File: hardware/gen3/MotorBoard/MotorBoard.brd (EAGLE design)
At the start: 140 x 107 mm, 193 parts, among them U2 ATMEGA165PV-8AU

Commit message: fixed ERCs on all boards
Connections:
- new net N$45: R2.2, SPI_HEADER.1
- net 5V: now also U$5.5, U$6.5, U$7.5, U$8.5; no longer U$5.2, U$6.2, U$7.2, U$8.2
- net GND: now also U$5.2, U$6.2, U$7.2, U$8.2; no longer U$5.5, U$6.5, U$7.5, U$8.5
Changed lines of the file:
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@@
 <contactref element="C15" pad="1"/>
 <contactref element="C24" pad="1"/>
-<contactref element="U$5" pad="5"/>
 <contactref element="R90" pad="1"/>
 <contactref element="C33" pad="1"/>
@@
 <contactref element="LED13" pad="C"/>
 <contactref element="LED15" pad="C"/>
-<contactref element="U$6" pad="5"/>
-<contactref element="U$7" pad="5"/>
 <contactref element="R60" pad="1"/>
-<contactref element="U$8" pad="5"/>
 <contactref element="R62" pad="1"/>
 <contactref element="R58" pad="1"/>
+<contactref element="U$5" pad="2"/>
+<contactref element="U$6" pad="2"/>
+<contactref element="U$7" pad="2"/>
+<contactref element="U$8" pad="2"/>
 <wire x1="137" y1="25.86" x2="137" y2="79.86" width="0" layer="19" extent="1-1"/>
 <wire x1="100.0766" y1="38.191" x2="137" y2="25.86" width="0" layer="19" extent="1-1"/>
@@
 <wire x1="24" y1="57" x2="52.77" y2="54.98" width="0" layer="19" extent="1-1"/>
 <wire x1="24" y1="59.54" x2="24" y2="57" width="0" layer="19" extent="1-1"/>
-<wire x1="14.43" y1="62.8801" x2="24" y2="59.54" width="0" layer="19" extent="16-16"/>
-<wire x1="14.17" y1="63.58" x2="14.43" y2="62.8801" width="0" layer="19" extent="16-16"/>
+<wire x1="13.48" y1="60.2799" x2="24" y2="59.54" width="0" layer="19" extent="16-16"/>
+<wire x1="14.17" y1="63.58" x2="13.48" y2="60.2799" width="0" layer="19" extent="16-16"/>
 <wire x1="13.73" y1="64.58" x2="14.17" y2="63.58" width="0" layer="19" extent="16-16"/>
 <wire x1="14.25" y1="65.58" x2="13.73" y2="64.58" width="0" layer="19" extent="16-16"/>
@@
 <wire x1="8.14" y1="75.52" x2="6.98" y2="74.52" width="0" layer="19" extent="16-16"/>
 <wire x1="6.82" y1="77.52" x2="8.14" y2="75.52" width="0" layer="19" extent="16-16"/>
-<wire x1="11.97" y1="52.71" x2="14.43" y2="62.8801" width="0" layer="19" extent="16-16"/>
+<wire x1="11.97" y1="52.71" x2="13.48" y2="60.2799" width="0" layer="19" extent="16-16"/>
 <wire x1="14.42" y1="49.9" x2="11.97" y2="52.71" width="0" layer="19" extent="16-16"/>
 <wire x1="8.16" y1="52.71" x2="11.97" y2="52.71" width="0" layer="19" extent="16-16"/>
@@
 <wire x1="16.35" y1="5.895" x2="13.429" y2="2.9234" width="0" layer="19" extent="16-16"/>
 <wire x1="63.34" y1="4.99" x2="97.105" y2="35.27" width="0" layer="19" extent="1-1"/>
-<wire x1="-96.95" y1="-1.6999" x2="1.569" y2="2.9234" width="0" layer="19" extent="1-16"/>
-<wire x1="-96.4" y1="-11" x2="-96.95" y2="-1.6999" width="0" layer="19" extent="1-1"/>
-<wire x1="-96.95" y1="-18.6999" x2="-96.4" y2="-11" width="0" layer="19" extent="1-1"/>
-<wire x1="-96.4" y1="-28" x2="-96.95" y2="-18.6999" width="0" layer="19" extent="1-1"/>
-<wire x1="-96.95" y1="-35.6999" x2="-96.4" y2="-28" width="0" layer="19" extent="1-1"/>
-<wire x1="-96.4" y1="-45" x2="-96.95" y2="-35.6999" width="0" layer="19" extent="1-1"/>
+<wire x1="-96" y1="-4.3001" x2="1.569" y2="2.9234" width="0" layer="19" extent="1-16"/>
+<wire x1="-96.4" y1="-11" x2="-96" y2="-4.3001" width="0" layer="19" extent="1-1"/>
+<wire x1="-96" y1="-21.3001" x2="-96.4" y2="-11" width="0" layer="19" extent="1-1"/>
+<wire x1="-96.4" y1="-28" x2="-96" y2="-21.3001" width="0" layer="19" extent="1-1"/>
+<wire x1="-96" y1="-38.3001" x2="-96.4" y2="-28" width="0" layer="19" extent="1-1"/>
+<wire x1="-96.4" y1="-45" x2="-96" y2="-38.3001" width="0" layer="19" extent="1-1"/>
 </signal>
 <signal name="3.3V">
@@
 <contactref element="R75" pad="2"/>
 <contactref element="R74" pad="2"/>
-<contactref element="U$5" pad="2"/>
-<contactref element="U$6" pad="2"/>
-<contactref element="U$7" pad="2"/>
-<contactref element="U$8" pad="2"/>
+<contactref element="U$5" pad="5"/>
+<contactref element="U$6" pad="5"/>
+<contactref element="U$7" pad="5"/>
+<contactref element="U$8" pad="5"/>
 <wire x1="137" y1="23.32" x2="137" y2="77.32" width="0" layer="19" extent="1-1"/>
 <wire x1="64.1" y1="60.61" x2="137" y2="77.32" width="0" layer="19" extent="1-1"/>
@@
 <wire x1="24" y1="67.16" x2="52.77" y2="52.44" width="0" layer="19" extent="1-1"/>
 <wire x1="24" y1="69.7" x2="24" y2="67.16" width="0" layer="19" extent="1-1"/>
-<wire x1="13.48" y1="60.2799" x2="24" y2="67.16" width="0" layer="19" extent="16-16"/>
-<wire x1="11.62" y1="46.09" x2="13.48" y2="60.2799" width="0" layer="19" extent="16-16"/>
+<wire x1="14.43" y1="62.8801" x2="24" y2="67.16" width="0" layer="19" extent="16-16"/>
+<wire x1="16.7" y1="46.09" x2="14.43" y2="62.8801" width="0" layer="19" extent="16-16"/>
+<wire x1="16.38" y1="45.09" x2="16.7" y2="46.09" width="0" layer="19" extent="16-16"/>
+<wire x1="16.02" y1="45.09" x2="16.38" y2="45.09" width="0" layer="19" extent="16-16"/>
+<wire x1="11.62" y1="46.09" x2="16.02" y2="45.09" width="0" layer="19" extent="16-16"/>
 <wire x1="11.26" y1="45.09" x2="11.62" y2="46.09" width="0" layer="19" extent="16-16"/>
 <wire x1="10.94" y1="45.09" x2="11.26" y2="45.09" width="0" layer="19" extent="16-16"/>
-<wire x1="16.02" y1="45.09" x2="11.62" y2="46.09" width="0" layer="19" extent="16-16"/>
-<wire x1="16.38" y1="45.09" x2="16.02" y2="45.09" width="0" layer="19" extent="16-16"/>
-<wire x1="16.7" y1="46.09" x2="16.38" y2="45.09" width="0" layer="19" extent="16-16"/>
 <wire x1="6.54" y1="46.09" x2="10.94" y2="45.09" width="0" layer="19" extent="16-16"/>
 <wire x1="6.18" y1="45.09" x2="6.54" y2="46.09" width="0" layer="19" extent="16-16"/>
@@
 <wire x1="1.1" y1="45.09" x2="1.46" y2="46.09" width="0" layer="19" extent="16-16"/>
 <wire x1="0.78" y1="45.09" x2="1.1" y2="45.09" width="0" layer="19" extent="16-16"/>
-<wire x1="-96" y1="-4.3001" x2="0.78" y2="45.09" width="0" layer="19" extent="1-16"/>
-<wire x1="-96" y1="-21.3001" x2="-96" y2="-4.3001" width="0" layer="19" extent="1-1"/>
-<wire x1="-96" y1="-38.3001" x2="-96" y2="-21.3001" width="0" layer="19" extent="1-1"/>
+<wire x1="-96.95" y1="-1.6999" x2="0.78" y2="45.09" width="0" layer="19" extent="1-16"/>
+<wire x1="-96.95" y1="-18.6999" x2="-96.95" y2="-1.6999" width="0" layer="19" extent="1-1"/>
+<wire x1="-96.95" y1="-35.6999" x2="-96.95" y2="-18.6999" width="0" layer="19" extent="1-1"/>
 </signal>
 <signal name="M1QB">
@@
 <wire x1="62.38" y1="90.9934" x2="116" y2="72.38" width="0" layer="19" extent="1-1"/>
 </signal>
+<signal name="N$45">
+<contactref element="SPI_HEADER" pad="1"/>
+<contactref element="R2" pad="2"/>
+<wire x1="13.98" y1="52.71" x2="116" y2="80" width="0" layer="19" extent="16-16"/>
+</signal>
 </signals>

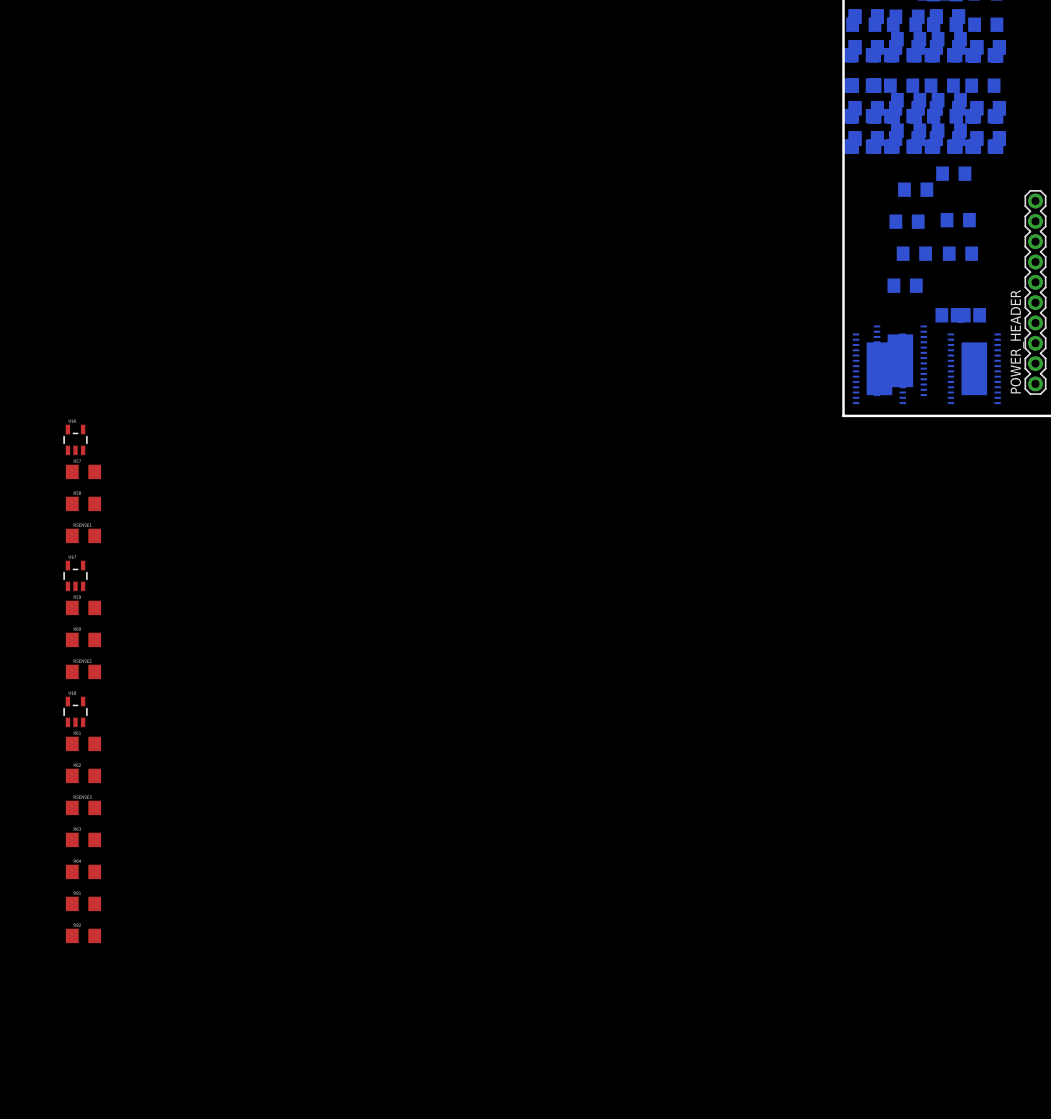
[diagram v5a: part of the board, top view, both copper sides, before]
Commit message: new overcurrent protection of pwm
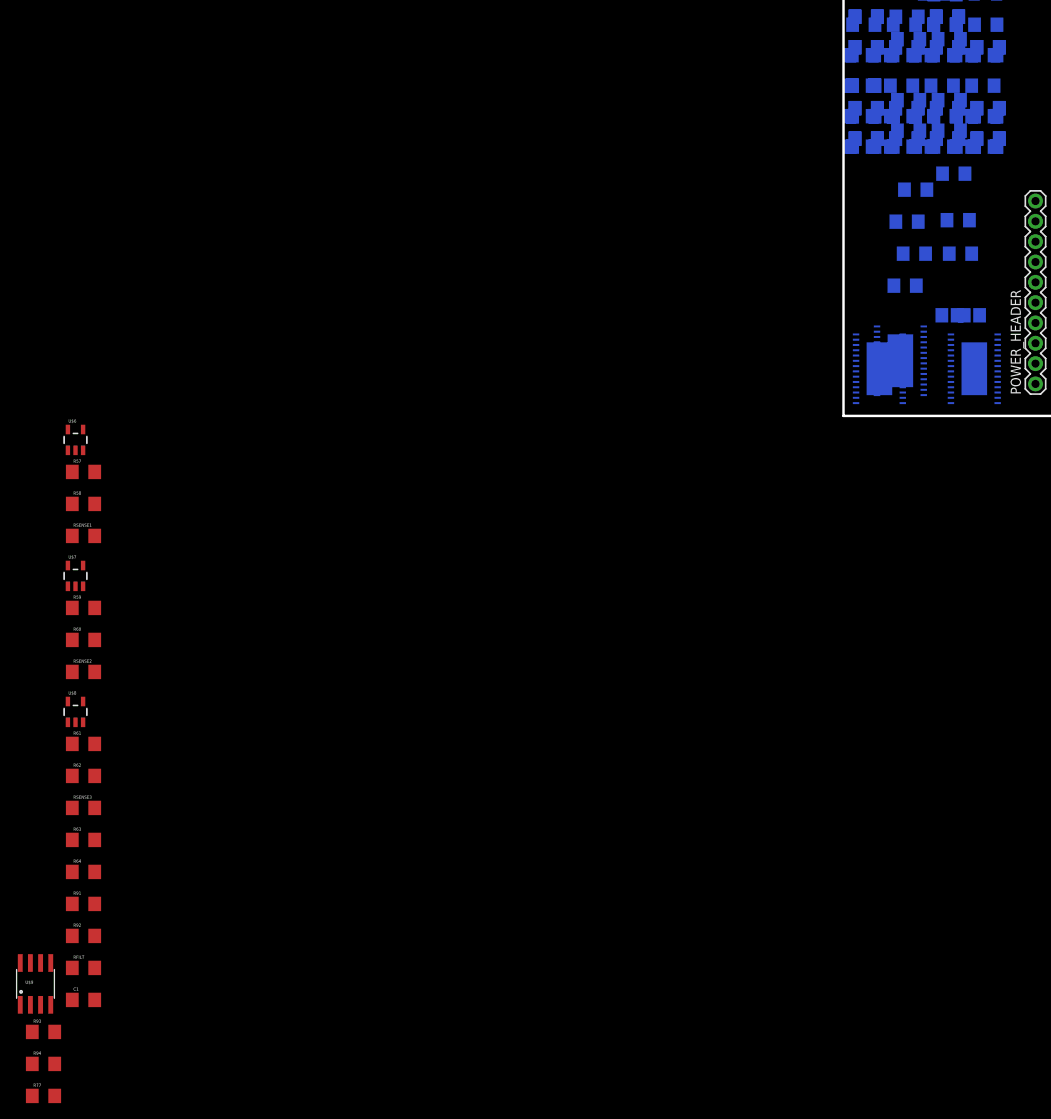
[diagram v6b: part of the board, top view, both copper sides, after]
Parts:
- added C1: .1uF, SparkFun-Passives:1206
- added R93: 64k, SparkFun-Resistors:1206
- added R94: 36k, SparkFun-Resistors:1206
- added RFILT: 15k, SparkFun-Resistors:1206
- added U$9: LM393, SparkFun-AnalogIC:SO08
- R77: value 1k -> 3k
- moved R77 175.5 mm to (-100.0, -85.0), flipped to the top
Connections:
- removed net N$97: R77.1, U$4.ENABLE
- new net LIM1: R77.2, U$4.ENABLE, U$9.1
- new net N$46: C1.1, RFILT.2, U$5.3
- new net N$66: R93.1, R94.2, U$9.2
- net 5V: now also R93.2, U$9.8
- net GND: now also C1.2, R94.1, U$9.4
- net O1: now also RFILT.1; no longer U$5.3
- net PWM1: now also R77.1; no longer R77.2
- net SENSE1: now also U$9.3
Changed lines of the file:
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@@
 <element name="R75" library="SparkFun-Resistors" package="1206" value="10k" x="7.58" y="45.09" rot="MR0"/>
 <element name="R76" library="SparkFun-Resistors" package="1206" value="10k" x="12.66" y="45.09" rot="MR0"/>
-<element name="R77" library="SparkFun-Resistors" package="1206" value="1k" x="17.74" y="45.09" rot="MR0"/>
 <element name="R78" library="SparkFun-Resistors" package="1206" value="1k" x="2.82" y="46.09" rot="MR0"/>
 <element name="R79" library="SparkFun-Resistors" package="1206" value="1k" x="7.9" y="46.09" rot="MR0"/>
@@
 <element name="R91" library="SparkFun-Resistors" package="1206" value="1k" x="-95" y="-61"/>
 <element name="R92" library="SparkFun-Resistors" package="1206" value="1k" x="-95" y="-65"/>
+<element name="RFILT" library="SparkFun-Resistors" package="1206" value="15k" x="-95" y="-69"/>
+<element name="C1" library="SparkFun-Passives" package="1206" value=".1uF" x="-95" y="-73"/>
+<element name="U$9" library="SparkFun-AnalogIC" package="SO08" value="LM393" x="-101" y="-71"/>
+<element name="R93" library="SparkFun-Resistors" package="1206" value="64k" x="-100" y="-77"/>
+<element name="R94" library="SparkFun-Resistors" package="1206" value="36k" x="-100" y="-81"/>
+<element name="R77" library="SparkFun-Resistors" package="1206" value="3k" x="-100" y="-85"/>
 </elements>
 <signals>
@@
 <contactref element="U$7" pad="2"/>
 <contactref element="U$8" pad="2"/>
+<contactref element="C1" pad="2"/>
+<contactref element="U$9" pad="4"/>
+<contactref element="R94" pad="1"/>
 <wire x1="137" y1="25.86" x2="137" y2="79.86" width="0" layer="19" extent="1-1"/>
 <wire x1="100.0766" y1="38.191" x2="137" y2="25.86" width="0" layer="19" extent="1-1"/>
@@
 <wire x1="-96" y1="-38.3001" x2="-96.4" y2="-28" width="0" layer="19" extent="1-1"/>
 <wire x1="-96.4" y1="-45" x2="-96" y2="-38.3001" width="0" layer="19" extent="1-1"/>
+<wire x1="-93.6" y1="-73" x2="-96.4" y2="-45" width="0" layer="19" extent="1-1"/>
+<wire x1="-99.095" y1="-73.6162" x2="-93.6" y2="-73" width="0" layer="19" extent="1-1"/>
+<wire x1="-101.4" y1="-81" x2="-99.095" y2="-73.6162" width="0" layer="19" extent="1-1"/>
 </signal>
 <signal name="3.3V">
@@
 <contactref element="U$7" pad="5"/>
 <contactref element="U$8" pad="5"/>
+<contactref element="U$9" pad="8"/>
+<contactref element="R93" pad="2"/>
 <wire x1="137" y1="23.32" x2="137" y2="77.32" width="0" layer="19" extent="1-1"/>
 <wire x1="64.1" y1="60.61" x2="137" y2="77.32" width="0" layer="19" extent="1-1"/>
@@
 <wire x1="-96.95" y1="-18.6999" x2="-96.95" y2="-1.6999" width="0" layer="19" extent="1-1"/>
 <wire x1="-96.95" y1="-35.6999" x2="-96.95" y2="-18.6999" width="0" layer="19" extent="1-1"/>
+<wire x1="-102.905" y1="-68.3838" x2="-96.95" y2="-35.6999" width="0" layer="19" extent="1-1"/>
+<wire x1="-98.6" y1="-77" x2="-102.905" y2="-68.3838" width="0" layer="19" extent="1-1"/>
 </signal>
 <signal name="M1QB">
@@
 <contactref element="R89" pad="2"/>
 <contactref element="U2" pad="61"/>
-<wire x1="14.43" y1="60.2799" x2="66.3932" y2="100.62" width="0" layer="19" extent="1-16"/>
-<wire x1="6.54" y1="49.9" x2="14.43" y2="60.2799" width="0" layer="19" extent="16-16"/>
+<contactref element="U$9" pad="3"/>
+<wire x1="6.54" y1="49.9" x2="-100.365" y2="-73.6162" width="0" layer="19" extent="1-16"/>
+<wire x1="14.43" y1="60.2799" x2="6.54" y2="49.9" width="0" layer="19" extent="16-16"/>
+<wire x1="66.3932" y1="100.62" x2="14.43" y2="60.2799" width="0" layer="19" extent="1-16"/>
 </signal>
 <signal name="SENSE2">
@@
 </signal>
 <signal name="PWM1">
-<contactref element="R77" pad="2"/>
 <contactref element="U2" pad="14"/>
-<wire x1="16.34" y1="45.09" x2="62.38" y2="88.6058" width="0" layer="19" extent="1-16"/>
+<contactref element="R77" pad="1"/>
+<wire x1="62.38" y1="88.6058" x2="-101.4" y2="-85" width="0" layer="19" extent="1-1"/>
 </signal>
 <signal name="PWM2">
@@
 <wire x1="11.58" y1="49.9" x2="77.62" y2="90.9934" width="0" layer="19" extent="1-16"/>
 </signal>
-<signal name="N$97">
-<contactref element="U$4" pad="ENABLE"/>
-<contactref element="R77" pad="1"/>
-<wire x1="13.429" y1="6.8858" x2="19.14" y2="45.09" width="0" layer="19" extent="16-16"/>
-</signal>
 <signal name="N$98">
 <contactref element="U$4" pad="DIR"/>
@@
 <contactref element="U$4" pad="LSS"/>
 <contactref element="RSENSE" pad="2"/>
-<contactref element="U$5" pad="3"/>
-<wire x1="34.54" y1="43.24" x2="33.68" y2="45.24" width="0" layer="19" extent="16-16"/>
-<wire x1="37.11" y1="25.24" x2="34.54" y2="43.24" width="0" layer="19" extent="16-16"/>
+<contactref element="RFILT" pad="1"/>
+<wire x1="19.271" y1="10.1878" x2="-96.4" y2="-69" width="0" layer="19" extent="1-16"/>
+<wire x1="37.11" y1="25.24" x2="19.271" y2="10.1878" width="0" layer="19" extent="16-16"/>
+<wire x1="34.54" y1="43.24" x2="37.11" y2="25.24" width="0" layer="19" extent="16-16"/>
+<wire x1="33.68" y1="45.24" x2="34.54" y2="43.24" width="0" layer="19" extent="16-16"/>
 <wire x1="16.7" y1="38.47" x2="33.68" y2="45.24" width="0" layer="19" extent="16-16"/>
 <wire x1="11.62" y1="38.47" x2="16.7" y2="38.47" width="0" layer="19" extent="16-16"/>
 <wire x1="6.54" y1="38.47" x2="11.62" y2="38.47" width="0" layer="19" extent="16-16"/>
 <wire x1="11.3" y1="52.71" x2="11.62" y2="38.47" width="0" layer="19" extent="16-16"/>
-<wire x1="12.53" y1="60.2799" x2="11.3" y2="52.71" width="0" layer="19" extent="16-16"/>
-<wire x1="19.271" y1="10.1878" x2="37.11" y2="25.24" width="0" layer="19" extent="16-16"/>
 </signal>
 <signal name="N$109">
@@
 <wire x1="13.98" y1="52.71" x2="116" y2="80" width="0" layer="19" extent="16-16"/>
 </signal>
+<signal name="N$46">
+<contactref element="RFILT" pad="2"/>
+<contactref element="C1" pad="1"/>
+<contactref element="U$5" pad="3"/>
+<wire x1="-93.6" y1="-69" x2="-96.4" y2="-73" width="0" layer="19" extent="1-1"/>
+<wire x1="12.53" y1="60.2799" x2="-93.6" y2="-69" width="0" layer="19" extent="1-16"/>
+</signal>
+<signal name="N$66">
+<contactref element="R93" pad="1"/>
+<contactref element="R94" pad="2"/>
+<contactref element="U$9" pad="2"/>
+<wire x1="-101.635" y1="-73.6162" x2="-101.4" y2="-77" width="0" layer="19" extent="1-1"/>
+<wire x1="-98.6" y1="-81" x2="-101.4" y2="-77" width="0" layer="19" extent="1-1"/>
+</signal>
+<signal name="LIM1">
+<contactref element="U$4" pad="ENABLE"/>
+<contactref element="U$9" pad="1"/>
+<contactref element="R77" pad="2"/>
+<wire x1="-102.905" y1="-73.6162" x2="-98.6" y2="-85" width="0" layer="19" extent="1-1"/>
+<wire x1="13.429" y1="6.8858" x2="-102.905" y2="-73.6162" width="0" layer="19" extent="1-16"/>
+</signal>
 </signals>
